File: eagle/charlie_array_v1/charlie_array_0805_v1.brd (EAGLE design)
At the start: 101.6 x 25.4 mm, 158 parts, among them IC1 MEGA8-AI, IC2 317EMP, J1 AVR_SPI_PRG_6, Q1 FA-128

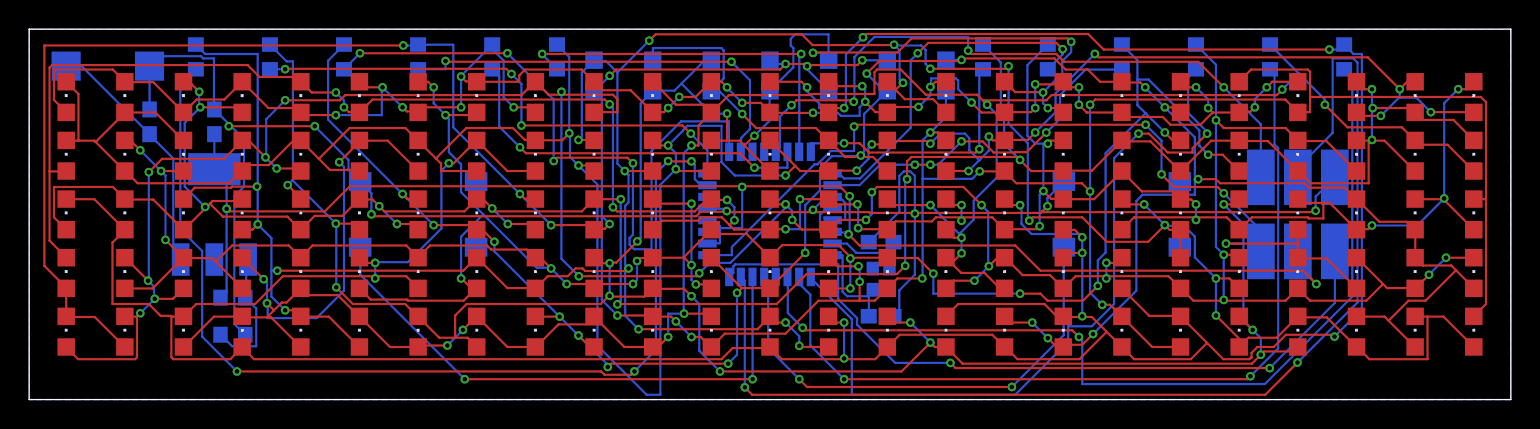
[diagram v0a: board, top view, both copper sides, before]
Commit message: adjusted to fit in 100mm width
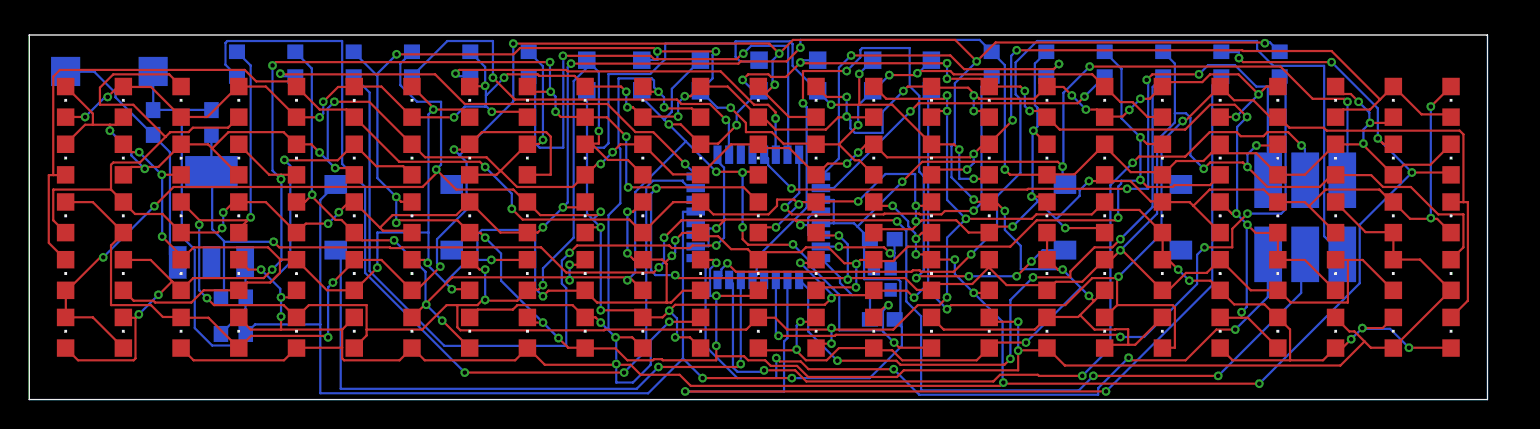
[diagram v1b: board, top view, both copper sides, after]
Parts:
- moved R8 4.45 mm to (85.8, 23.0)
- moved R7 3.38 mm to (81.8, 23.0)
- moved R9 2.86 mm to (14.2, 23.0)
- moved R6 2.30 mm to (77.8, 23.0)
- moved R2 2.01 mm to (34.2, 23.0)
- moved R10 1.81 mm to (18.2, 23.0)
- moved UPSW 1.68 mm to (25.0, 12.5)
- moved L2_4 1.59 mm to (97.5, 20.4)
- moved L7_3 1.58 mm to (97.5, 16.5)
- moved R1 1.58 mm to (30.2, 23.0)
- moved L4_12 1.57 mm to (97.5, 12.5)
- moved L11_6 1.57 mm to (97.5, 8.54)
- moved L9_12 1.56 mm to (97.5, 4.58)
- moved L3_2 1.53 mm to (93.5, 20.4)
- moved L3_7 1.52 mm to (93.5, 16.5)
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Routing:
- net DR7: track 184.4 -> 227.0 mm, vias 14 -> 21
- net DR2: track 188.0 -> 149.8 mm, vias 15 -> 14
- net DR8: track 249.3 -> 211.8 mm, vias 14 -> 16
- net GNDA: track 136.0 -> 166.5 mm, vias 8 -> 6
- net DR10: track 205.8 -> 181.6 mm, vias 20 -> 25
- net MISO: track 52.2 -> 69.9 mm
- net N$3: track 33.9 -> 51.6 mm, vias 2 -> 6
- net MOSI: track 80.0 -> 62.4 mm, vias 2 -> 4
- net DR9: track 208.9 -> 194.8 mm, vias 20 -> 18
- net DR11: track 186.4 -> 199.2 mm, vias 19 -> 17
- net DR6: track 196.2 -> 207.6 mm, vias 24 -> 18
- net D2: track 26.0 -> 36.5 mm
- net D7: track 58.3 -> 68.3 mm
- net D8: track 63.3 -> 53.6 mm, vias 2 -> 4
- net DR4: track 178.2 -> 168.6 mm, vias 20 -> 14
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- removed copper zone on layer 16, net GNDA
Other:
- board size 101.6 x 25.4 mm -> 100 x 25 mm
- board text added: "0805 charlie array v1"
- board text added: "bryan duxbury 8/26/2013"
